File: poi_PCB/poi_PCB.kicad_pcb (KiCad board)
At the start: 2 copper layers, 56 parts, among them J1 BATT_CONN, J4 USB_C_Receptacle_USB2.0, Q1 Q_NMOS_DGS, Q2 UMH3N, Q3 Q_NMOS_DGS, SW1 PWR_ON, U1 MT3608, U2 CH340G, U3 AMS1117-3.3, U4 ESP-12E, U5 TP4056, Y1 12MHz

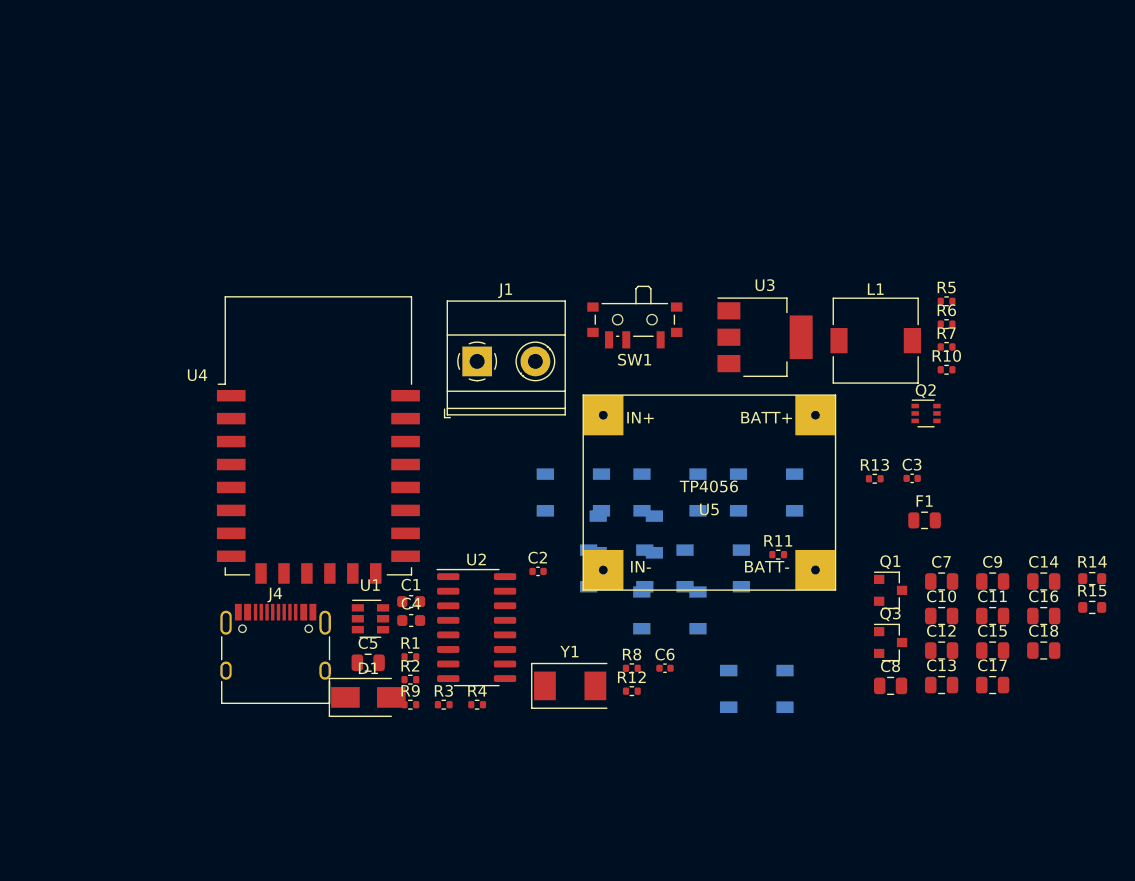
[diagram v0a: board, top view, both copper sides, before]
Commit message: Changed USB-> Serial chip, added documentation
-CH340G replaced with CH340C to eliminate the need for a crystal
-Part sourcing updated in BOM
-minor edits based on available parts
-Schematic updated to reflect changes
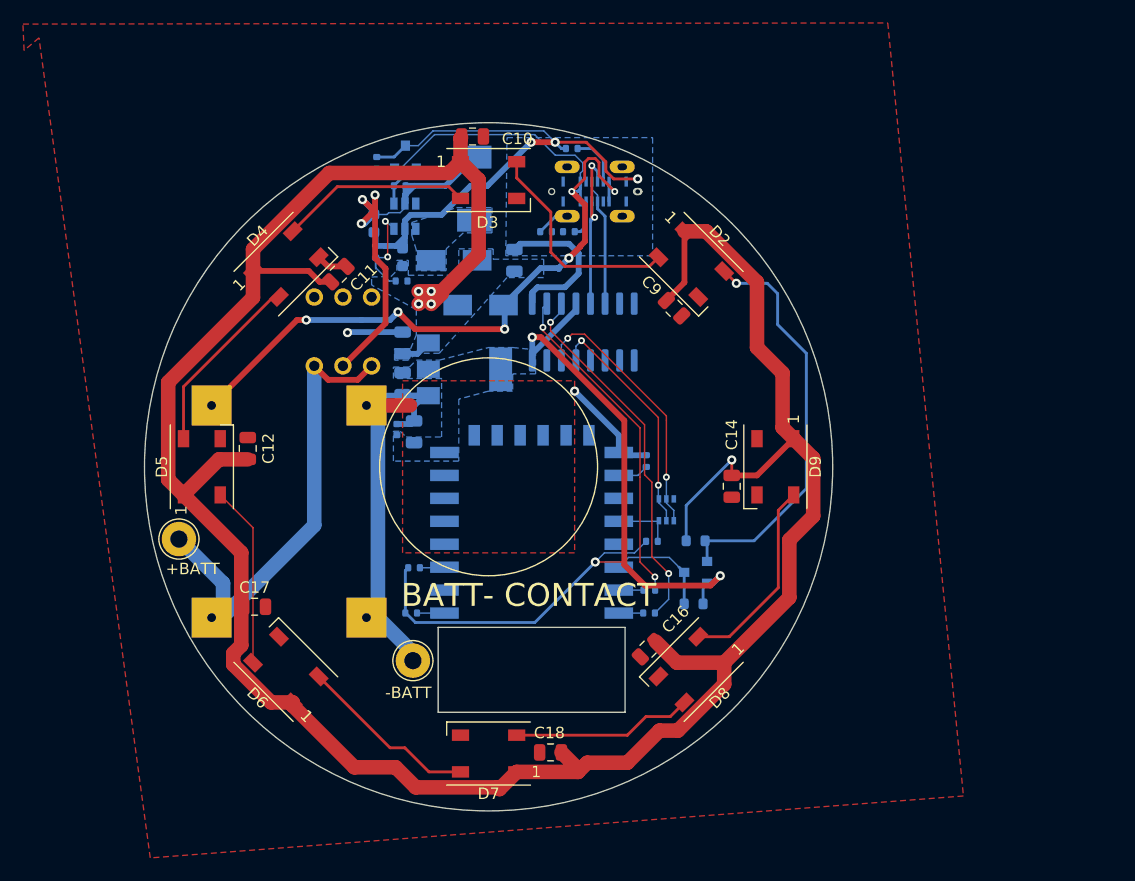
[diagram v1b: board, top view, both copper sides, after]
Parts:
- removed C13, C15: 10uF, Capacitor_SMD:C_0805_2012Metric
- removed C3: 22pF, Capacitor_SMD:C_0402_1005Metric
- removed F1: 2A_polyfuse, Fuse:Fuse_0805_2012Metric
- removed J1: BATT_CONN, TerminalBlock_Phoenix:TerminalBlock_Phoenix_MKDS-1,5-2-5.08_1x02_P5.08mm_Horizontal
- removed Y1: 12MHz, Crystal:Crystal_SMD_0603-2Pin_6.0x3.5mm
- added +BATT: TestPoint, TestPoint:TestPoint_THTPad_D3.0mm_Drill1.5mm, F.Cu at (80.5, 83.8)
- added -BATT: TestPoint, TestPoint:TestPoint_THTPad_D3.0mm_Drill1.5mm, F.Cu at (100.9, 94.4)
- added D10: D_Schottky_Small, Diode_SMD:D_SMA, B.Cu at (106.8, 63.4)
- C1, C4, C5, C6, C7, C8, D1, Q1, Q2, Q3, R1, R10, R11, R12, R13, R14, R15, R2, R3, R4, R5, R6, R7, R8, R9, U1, U3, U4, U5: moved to B.Cu
- C2: value 22pF -> 10uF; footprint Capacitor_SMD:C_0402_1005Metric -> Capacitor_SMD:C_0805_2012Metric; moved to B.Cu
- D2, D9: moved to F.Cu
- D3: renamed from D4; moved to F.Cu
- D4: renamed from D6; moved to F.Cu
- D5: renamed from D8; moved to F.Cu
- D6: renamed from D3; moved to F.Cu
- D7: renamed from D5; moved to F.Cu
- D8: renamed from D7; moved to F.Cu
- J4: footprint Connector_USB:USB_C_Receptacle_HRO_TYPE-C-31-M-12 -> USB4120-03-C_REVA:GCT_USB4120-03-C_REVA; moved to B.Cu
- L1: footprint Inductor_SMD:L_7.3x7.3_H3.5 -> Inductor_SMD:L_6.3x6.3_H3; moved to B.Cu
- SW1: value PWR_ON -> SW_Push_DPDT_8mm; footprint Button_Switch_SMD:SW_SPDT_PCM12 -> 8mm_switch:8mm_latching_switch; moved to B.Cu
- U2: value CH340G -> CH340C; moved to B.Cu
- moved C17 64.7 mm to (87.1, 89.7)
- moved C11 64.4 mm to (94.4, 60.7), turned to 45 degrees
- moved C12 63.0 mm to (86.5, 75.9), turned to 90 degrees
- moved C10 58.5 mm to (106.1, 48.7)
- moved Q1 56.7 mm to (100.2, 50.5), turned to 90 degrees
- moved R7 52.2 mm to (97.8, 51.0), turned to 270 degrees
- moved D5 52.1 mm to (82.5, 77.5), turned to 90 degrees
- moved C7 51.4 mm to (100.0, 66.7), turned to 90 degrees
- moved R10 51.3 mm to (100.8, 90.2), turned to 180 degrees
- moved R6 50.2 mm to (97.7, 58.8), turned to 90 degrees
- moved C8 50.0 mm to (100.0, 70.2), turned to 270 degrees
- moved J4 49.3 mm to (116.8, 53.5)
- moved R4 49.2 mm to (114.8, 49.8), turned to 180 degrees
- moved R5 47.6 mm to (99.9, 61.3), turned to 180 degrees
- moved D4 45.1 mm to (89.8, 59.8), turned to 45 degrees
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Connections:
- C10 pad 1: VCC -> +5V
- C11 pad 1: VCC -> +5V
- C12 pad 1: VCC -> +5V
- C14 pad 1: VCC -> +5V
- C16 pad 1: VCC -> +5V
- C17 pad 1: VCC -> +5V
- C18 pad 1: VCC -> +5V
- C2 pad 1: Net-(C2-Pad1) -> +5V
- C9 pad 1: VCC -> +5V
- Q2 pad 3: (no net) -> /GPIO0
- R12 pad 2: Net-(R12-Pad2) -> /GPIO0
- SW1 pad 1: Net-(C1-Pad2) -> +BATT
- SW1 pad 2: +BATT -> Net-(C1-Pad2)
- SW1 pad 3: (no net) -> +BATT
- U2 pad 7: Net-(C2-Pad1) -> (no net)
- U2 pad 8: Net-(C3-Pad1) -> (no net)
- U4 pad 18: Net-(R12-Pad2) -> /GPIO0
- U4 pad 20: (no net) -> /LED_SIG_3.3
- U5 pad 1: (no net) -> -BATT
- U5 pad 2: (no net) -> /VBUS
- U5 pad 3: (no net) -> +BATT
- U5 pad 4: (no net) -> -BATT
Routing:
- net +5V: track 0.00 -> 233.7 mm, vias 0 -> 5
- net -BATT: track 0.00 -> 122.3 mm, vias 0 -> 5
- net /VBUS: track 0.00 -> 81.2 mm, vias 0 -> 6
- net +3V3: track 0.00 -> 76.0 mm, vias 0 -> 3
- net +BATT: track 0.00 -> 39.9 mm
- net Net-(C1-Pad2): track 0.00 -> 39.0 mm, vias 0 -> 3
- net /LED_SIG_5: track 0.00 -> 36.1 mm, vias 0 -> 1
- net Net-(R9-Pad1): track 0.00 -> 32.3 mm, vias 0 -> 2
- net Net-(R8-Pad2): track 0.00 -> 29.2 mm, vias 0 -> 2
- net /RTS: track 0.00 -> 23.3 mm, vias 0 -> 2
- net /DTR: track 0.00 -> 20.7 mm, vias 0 -> 2
- net Net-(D2-Pad2): track 0.00 -> 19.4 mm
- net Net-(D8-Pad2): track 0.00 -> 17.4 mm
- net Net-(D3-Pad2): track 0.00 -> 16.7 mm
- net Net-(D4-Pad2): track 0.00 -> 16.1 mm
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- added copper zone on B.Cu, net +3V3
- added copper zone on B.Cu, net +5V
- added copper zone on B.Cu, net -BATT
- added copper zone on F.Cu, net -BATT
- added copper zone on B.Cu, net Net-(D1-Pad2)
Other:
- board outline added: 60 x 60 mm
- rule trace_min: 0.2 -> 0.127
- rule via_min_size: 0.4 -> 0.6
- board text added: "BATT- CONTACT"

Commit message: Added mounting holes
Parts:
- added H1: MountingHole, MountingHole:MountingHole_3.2mm_M3, F.Cu at (129.0, 67.0)
- added H2: MountingHole, MountingHole:MountingHole_3.2mm_M3, F.Cu at (86.0, 66.6)
- added H3: MountingHole, MountingHole:MountingHole_3.2mm_M3, F.Cu at (100.0, 100.3)
- moved C16 1.45 mm to (122.5, 92.5)
- renumbered +BATT to +BATT1, -BATT to -BATT1
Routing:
- net /VBUS: track 81.2 -> 84.0 mm
- net Net-(D4-Pad2): track 16.1 -> 18.5 mm
- net Net-(D7-Pad2): track 15.8 -> 17.1 mm
- net Net-(D6-Pad2): track 15.8 -> 17.0 mm
- net Net-(R5-Pad2): track 9.36 -> 8.38 mm
- net Net-(R8-Pad2): track 29.2 -> 30.1 mm

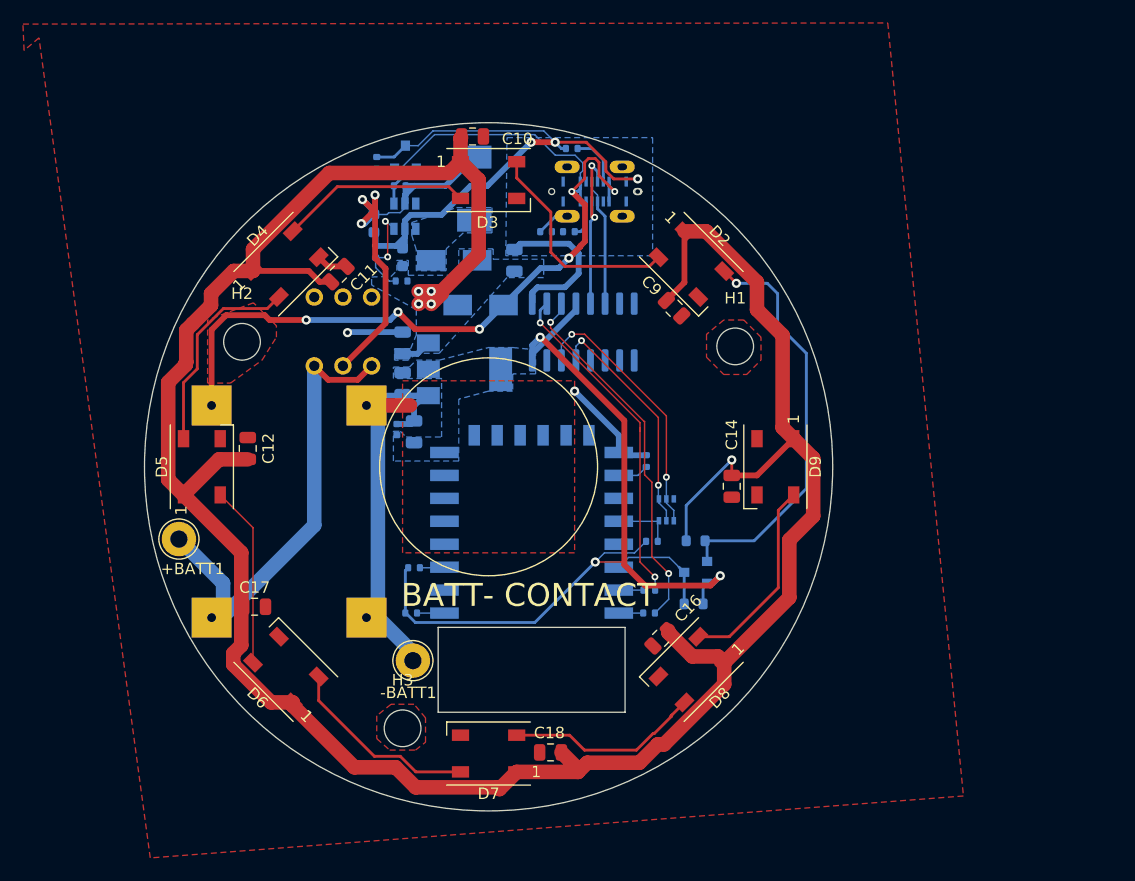
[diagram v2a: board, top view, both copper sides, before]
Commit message: Verified reset circuit
Breadboarded and edited reset circuit.
-USBC port moved closer to center
-transistors replaced because of issues with transistor quality
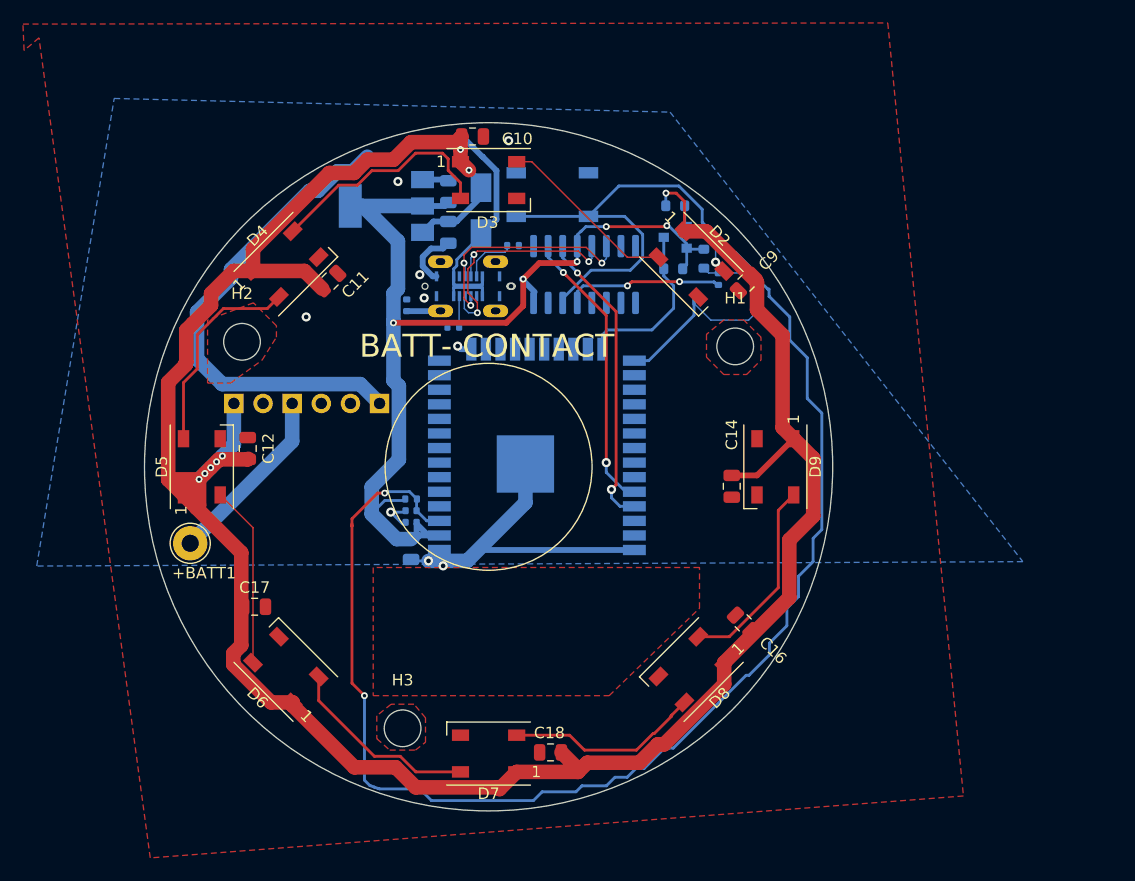
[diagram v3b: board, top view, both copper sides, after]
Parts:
- removed -BATT1: TestPoint, TestPoint:TestPoint_THTPad_D3.0mm_Drill1.5mm
- removed C2: 10uF, Capacitor_SMD:C_0805_2012Metric
- removed C4: 22uF, Capacitor_SMD:C_0603_1608Metric
- removed D1: D_Schottky, Diode_SMD:D_SMA
- removed L1: 22uH, Inductor_SMD:L_6.3x6.3_H3
- removed Q1: Q_NMOS_DGS, Package_TO_SOT_SMD:SOT-23
- removed Q2: UMH3N, Package_TO_SOT_SMD:SOT-363_SC-70-6
- removed R11, R12, R13, R7: 10K, Resistor_SMD:R_0402_1005Metric
- removed R5: 73K, Resistor_SMD:R_0402_1005Metric
- removed R8, R9: 470, Resistor_SMD:R_0402_1005Metric
- removed U4: ESP-12E, RF_Module:ESP-12E
- removed U5: TP4056, Arduino:TP4056
- added U6: MH-CD42, Arduino:MH-CD42, B.Cu at (85.3, 72.0)
- C1: value 22uF -> 1uF; footprint Capacitor_SMD:C_0603_1608Metric -> Capacitor_SMD:C_0402_1005Metric
- R2: value 10K -> 220
- R6: footprint Resistor_SMD:R_0402_1005Metric -> Resistor_SMD:R_0603_1608Metric
- SW1: value SW_Push_DPDT_8mm -> SW_Push; footprint 8mm_switch:8mm_latching_switch -> Button_Switch_SMD:SW_SPST_TL3342
- U1: value MT3608 -> ESP32-WROOM-32D; footprint Package_TO_SOT_SMD:SOT-23-6 -> RF_Module:ESP32-WROOM-32
- moved Q3 29.3 mm to (123.8, 57.5)
- moved R14 29.3 mm to (123.8, 54.7)
- moved R15 29.3 mm to (123.6, 60.2)
- moved R2 29.0 mm to (127.5, 61.1), turned to 270 degrees
- moved R6 28.6 mm to (126.3, 59.4), turned to 270 degrees
- moved C1 25.3 mm to (100.7, 81.3), turned to 180 degrees
- moved U1 23.8 mm to (111.7, 76.5), turned to 0 degrees
- moved SW1 21.7 mm to (113.1, 53.8), turned to 0 degrees
- moved C8 17.2 mm to (104.0, 53.5), turned to 90 degrees
- moved U3 15.8 mm to (98.6, 54.8), turned to 180 degrees
- moved J4 13.8 mm to (105.7, 61.8)
- moved R1 13.7 mm to (100.4, 63.4), turned to 90 degrees
- moved R3 13.1 mm to (104.4, 65.3)
- moved C7 10.4 mm to (104.0, 57.1), turned to 270 degrees
- moved C5 10.2 mm to (100.7, 84.6), turned to 270 degrees
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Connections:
- C1 pad 1: -BATT -> /RST
- C1 pad 2: Net-(C1-Pad2) -> GND
- C10 pad 2: -BATT -> GND
- C11 pad 2: -BATT -> GND
- C12 pad 2: -BATT -> GND
- C14 pad 2: -BATT -> GND
- C16 pad 2: -BATT -> GND
- C17 pad 2: -BATT -> GND
- C18 pad 2: -BATT -> GND
- C5 pad 2: -BATT -> GND
- C6 pad 2: -BATT -> GND
- C7 pad 2: -BATT -> GND
- C8 pad 2: -BATT -> GND
- C9 pad 2: -BATT -> GND
- D2 pad 3: -BATT -> GND
- D3 pad 3: -BATT -> GND
- D4 pad 3: -BATT -> GND
- D5 pad 3: -BATT -> GND
- D6 pad 3: -BATT -> GND
- D7 pad 3: -BATT -> GND
- D8 pad 3: -BATT -> GND
- D9 pad 3: -BATT -> GND
- J4 pad A1: -BATT -> GND
- J4 pad A12: -BATT -> GND
- J4 pad B1: -BATT -> GND
- J4 pad B12: -BATT -> GND
- R1 pad 2: -BATT -> GND
- R10 pad 1: Net-(R10-Pad1) -> /RST
- R2 pad 1: /boost_en_H -> /GPIO0
- R2 pad 2: Net-(C1-Pad2) -> Net-(R2-Pad2)
- R3 pad 1: -BATT -> GND
- R4 pad 2: -BATT -> GND
- R6 pad 1: Net-(R5-Pad2) -> +3V3
- R6 pad 2: -BATT -> /GPIO0
- SW1 pad 1: +BATT -> /RST
- SW1 pad 2: Net-(C1-Pad2) -> GND
- U1 pad 1: Net-(D1-Pad2) -> GND
- U1 pad 2: -BATT -> +3V3
- U1 pad 3: Net-(R5-Pad2) -> /RST
- U1 pad 4: /boost_en_H -> (no net)
- U1 pad 5: Net-(C1-Pad2) -> (no net)
- U2 pad 1: -BATT -> GND
- U2 pad 13: /DTR -> Net-(R2-Pad2)
- U2 pad 14: /RTS -> /RST
- U2 pad 2: Net-(R8-Pad2) -> /TXD
- U2 pad 3: Net-(R9-Pad1) -> /RXD
- U3 pad 1: -BATT -> GND
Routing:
- net /RST: track 0.00 -> 155.4 mm, vias 0 -> 2
- net -BATT: track 122.3 -> 0.00 mm, vias 5 -> 0
- net GND: track 0.00 -> 45.1 mm, vias 0 -> 9
- net Net-(C1-Pad2): track 39.0 -> 0.00 mm, vias 3 -> 0
- net Net-(R9-Pad1): track 32.3 -> 0.00 mm, vias 2 -> 0
- net Net-(R8-Pad2): track 30.1 -> 0.00 mm, vias 2 -> 0
- net /LED_SIG_5: track 36.1 -> 7.77 mm
- net /RXD: track 2.13 -> 26.4 mm, vias 0 -> 2
- net +BATT: track 39.9 -> 15.9 mm
- net /RTS: track 23.2 -> 0.00 mm, vias 2 -> 0
- net /TXD: track 2.15 -> 25.0 mm, vias 0 -> 2
- net /DTR: track 20.7 -> 0.00 mm, vias 2 -> 0
- net /GPIO0: track 5.36 -> 23.9 mm
- net +3V3: track 75.5 -> 93.2 mm, vias 3 -> 5
- net Net-(R2-Pad2): track 0.00 -> 13.8 mm, vias 0 -> 2
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- added copper zone on B.Cu, net GND
- added copper zone on F.Cu, net GND
- removed copper zone on B.Cu, net +3V3
- removed copper zone on B.Cu, net +5V
- removed copper zone on B.Cu, net -BATT
- removed copper zone on F.Cu, net -BATT
- removed copper zone on B.Cu, net Net-(D1-Pad2)
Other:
- outline, holes or cut-outs redrawn
